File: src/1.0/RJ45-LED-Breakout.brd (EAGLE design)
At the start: 16.5 x 27.9 mm, 5 parts, among them J1 RJ45-RJHSE-5481

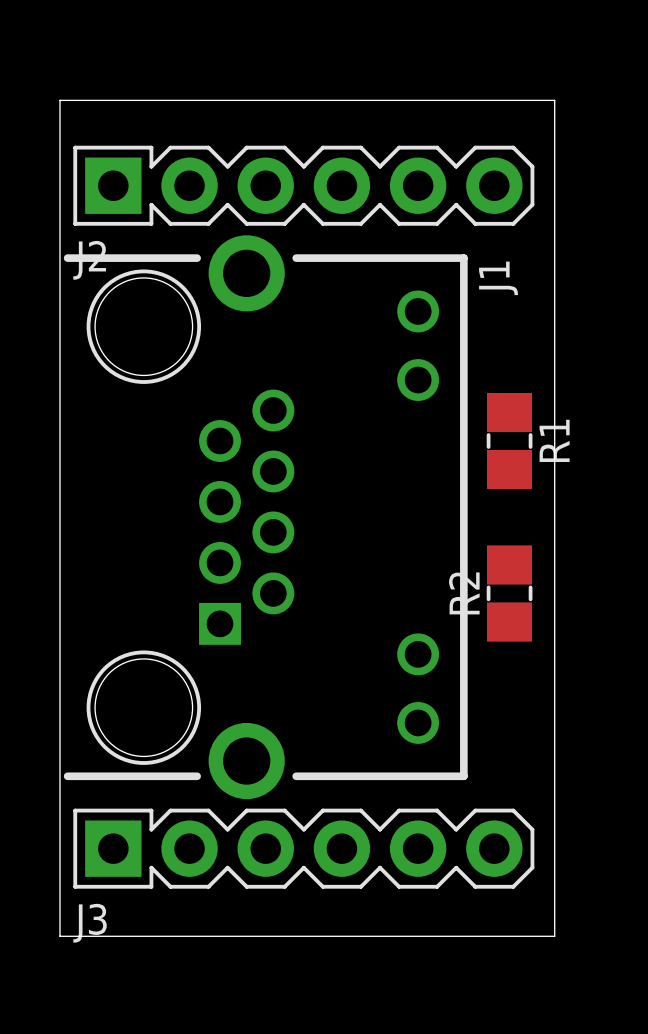
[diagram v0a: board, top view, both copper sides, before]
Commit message: Board mostly laid out but pins 7/8 are switched. Fix that then reroute and it is basicaly done. Need to add some more info on silk.
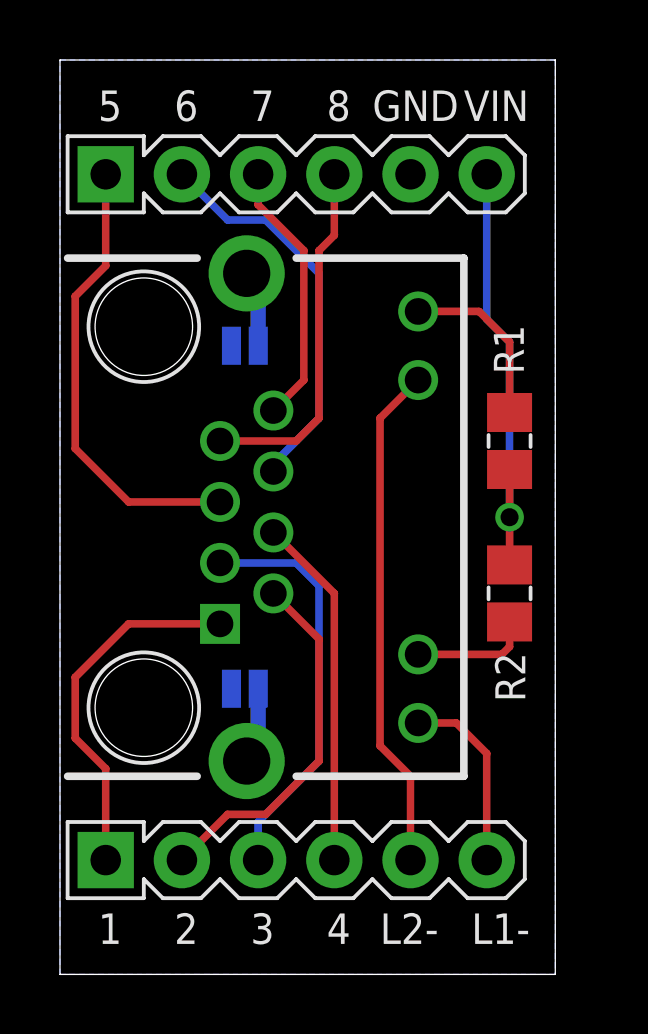
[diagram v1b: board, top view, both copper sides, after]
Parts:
- added SJ1, SJ2: (no value), LoganSmith-Connectors:SJ_2
- J2, J3: value (none) -> M06SQ1
- R1, R2: value R-0805 -> 1k
- moved J2 0.46 mm to (1.52, 25.4)
- moved J3 0.46 mm to (1.52, 2.54)
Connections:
- net N$10 renamed LED1+
- net N$9 renamed LED2+
- new net N$12: J1.SHEILD@1, SJ2.1
- net GND: now also J2.5, SJ1.2, SJ2.2; no longer J2.6
- net N$1: now also J1.5; no longer J1.7
- net N$11: now also SJ1.1; no longer J1.SHEILD@1
- net N$2: now also J1.6; no longer J1.8
- net N$3: now also J1.8; no longer J1.6
- net N$4: now also J1.7; no longer J1.5
- net N$5: now also J3.4; no longer J3.1
- net N$6: now also J3.3; no longer J3.2
- net N$7: now also J3.2; no longer J3.3
- net N$8: now also J3.1; no longer J3.4
- net VIN: now also J2.6; no longer J2.5
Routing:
- net LED2-: track 0.00 -> 16.9 mm
- net N$1: track 0.00 -> 15.1 mm
- net VIN: track 0.00 -> 14.9 mm, vias 0 -> 1
- net N$6: track 0.00 -> 13.6 mm
- net N$2: track 0.00 -> 13.2 mm
- net N$7: track 0.00 -> 12.2 mm
- net N$8: track 0.00 -> 12.1 mm
- net N$4: track 0.00 -> 12.0 mm
- net N$5: track 0.00 -> 11.8 mm
- net N$3: track 0.00 -> 8.93 mm
- net LED1-: track 0.00 -> 6.26 mm
- net LED2+: track 0.00 -> 5.82 mm
- net LED1+: track 0.00 -> 3.98 mm
- net N$11: track 0.00 -> 2.57 mm
- net N$12: track 0.00 -> 2.57 mm
- added copper zone on layer 16, net GND
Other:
- board size 16.5 x 27.9 mm -> 16.5 x 30.5 mm
- board text added: "1"
- board text added: "2"
- board text added: "3"
- board text added: "4"
- board text added: "5"
- board text added: "6"
- board text added: "7"
- board text added: "8"
- board text added: "GND"
- board text added: "L1-"
- board text added: "L2-"
- board text added: "VIN"
